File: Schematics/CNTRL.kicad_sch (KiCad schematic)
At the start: 14 parts, among them SW1 RotaryEncoder_Switch, SW2 RotaryEncoder_Switch, SW3 RotaryEncoder_Switch, U5 MCP23017_SP

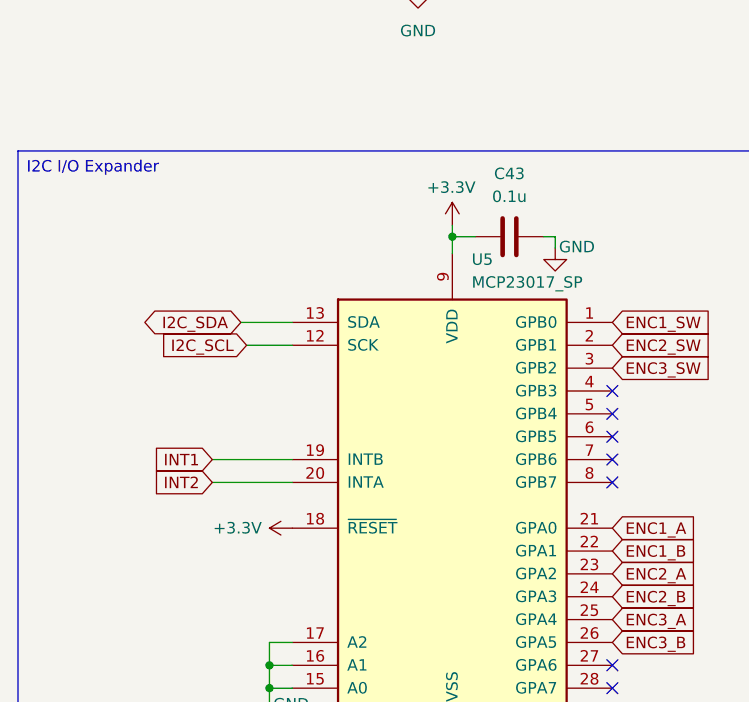
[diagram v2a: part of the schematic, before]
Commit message: Finished PCB routing
New Layout fits perfectly, now all the parts are through-hole and routed together. 20 Vias is a nightmare but better than what we started with
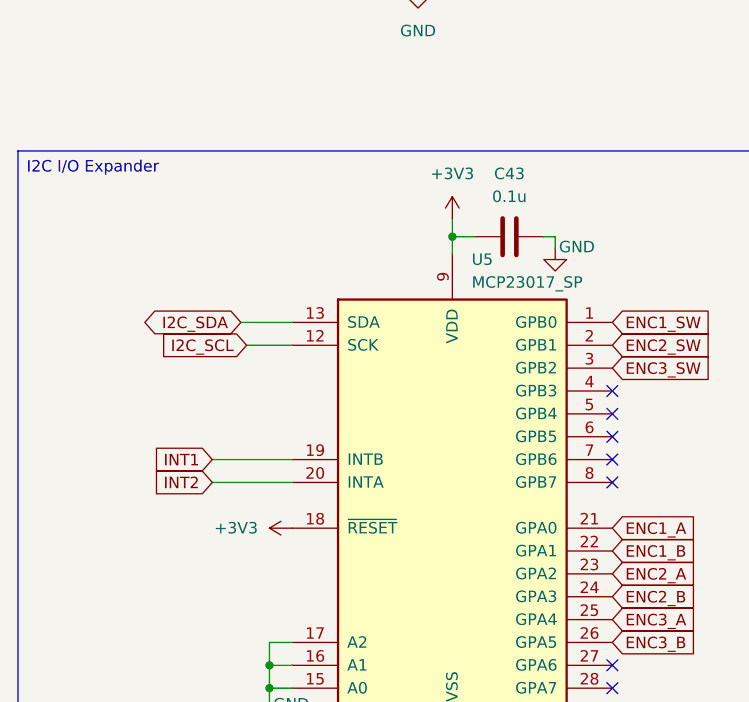
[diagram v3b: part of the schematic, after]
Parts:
- C43: footprint Capacitor_SMD:C_0805_2012Metric_Pad1.18x1.45mm_HandSolder -> Capacitor_THT:C_Disc_D4.7mm_W2.5mm_P5.00mm
- R34, R35, R36, R37, R38, R39, R46, R47, R48: footprint Resistor_SMD:R_0805_2012Metric_Pad1.20x1.40mm_HandSolder -> Resistor_THT:R_Axial_DIN0207_L6.3mm_D2.5mm_P10.16mm_Horizontal
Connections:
- net +3.3V is gone; now on net +3V3: C43.2, U5.18 (~{RESET}), U5.9 (VDD)
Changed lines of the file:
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@@
-	(wire
-		(pts
-			(xy 63.5 130.175) (xy 63.5 131.445)
-		)
-		(stroke
-			(width 0)
-			(type default)
-		)
-	)
 	(wire
 		(pts
@@
 		(pts
 			(xy 151.13 48.895) (xy 190.5 48.895)
+		)
+		(stroke
+			(width 0)
+			(type default)
+		)
+	)
+	(wire
+		(pts
+			(xy 63.5 129.54) (xy 63.5 131.445)
 		)
 		(stroke
@@
 			)
 		)
-		(property "Footprint" "Resistor_SMD:R_0805_2012Metric_Pad1.20x1.40mm_HandSolder"
+		(property "Footprint" "Resistor_THT:R_Axial_DIN0207_L6.3mm_D2.5mm_P10.16mm_Horizontal"
 			(at 46.228 81.915 90)
 			(effects
@@
 			)
 		)
-		(property "Footprint" "Resistor_SMD:R_0805_2012Metric_Pad1.20x1.40mm_HandSolder"
+		(property "Footprint" "Resistor_THT:R_Axial_DIN0207_L6.3mm_D2.5mm_P10.16mm_Horizontal"
 			(at 182.118 40.005 90)
 			(effects
@@
 	)
 	(symbol
-		(lib_id "power:+3.3V")
+		(lib_id "power:+3V3")
+		(at 73.66 36.195 0)
+		(unit 1)
+		(exclude_from_sim no)
+		(in_bom yes)
+		(on_board yes)
+		(dnp no)
+		(fields_autoplaced yes)
+		(property "Reference" "#PWR052"
+			(at 73.66 40.005 0)
+			(effects
+				(font
+					(size 1.27 1.27)
+				)
+				(hide yes)
+			)
+		)
+		(property "Value" "+3V3"
+			(at 73.66 31.115 0)
+			(effects
+				(font
+					(size 1.27 1.27)
+				)
+			)
+		)
+		(property "Footprint" ""
+			(at 73.66 36.195 0)
+			(effects
+				(font
+					(size 1.27 1.27)
+				)
+				(hide yes)
+			)
+		)
+		(property "Datasheet" ""
+			(at 73.66 36.195 0)
+			(effects
+				(font
+					(size 1.27 1.27)
+				)
+				(hide yes)
+			)
+		)
+		(property "Description" "Power symbol creates a global label with name \"+3V3\""
+			(at 73.66 36.195 0)
+			(effects
+				(font
+					(size 1.27 1.27)
+				)
+				(hide yes)
+			)
+		)
+		(pin "1"
+		)
+		(instances
+			(project "Harmoniser HAT"
+				(path "/41751dd2-97f9-4cc6-b9e6-b561e5949053/5d678f4e-03b5-43f5-b100-a64e850a5e5c"
+					(reference "#PWR052")
+					(unit 1)
+				)
+			)
+		)
+	)
+	(symbol
+		(lib_id "power:+3V3")
 		(at 45.72 163.83 90)
 		(unit 1)
@@
 		(on_board yes)
 		(dnp no)
-		(property "Reference" "#PWR0183"
+		(fields_autoplaced yes)
+		(property "Reference" "#PWR018"
 			(at 49.53 163.83 0)
 			(effects
@@
 			)
 		)
-		(property "Value" "+3.3V"
-			(at 39.624 163.83 90)
-			(effects
-				(font
-					(size 1.27 1.27)
-				)
+		(property "Value" "+3V3"
+			(at 41.91 163.8299 90)
+			(effects
+				(font
+					(size 1.27 1.27)
+				)
+				(justify left)
 			)
 		)
@@
 			)
 		)
-		(property "Description" "Power symbol creates a global label with name \"+3.3V\""
+		(property "Description" "Power symbol creates a global label with name \"+3V3\""
 			(at 45.72 163.83 0)
 			(effects
@@
 			(project "Harmoniser HAT"
 				(path "/41751dd2-97f9-4cc6-b9e6-b561e5949053/5d678f4e-03b5-43f5-b100-a64e850a5e5c"
-					(reference "#PWR0183")
-					(unit 1)
-				)
-			)
-		)
-	)
-	(symbol
-		(lib_id "power:+3V3")
-		(at 73.66 36.195 0)
-		(unit 1)
-		(exclude_from_sim no)
-		(in_bom yes)
-		(on_board yes)
-		(dnp no)
-		(fields_autoplaced yes)
-		(property "Reference" "#PWR052"
-			(at 73.66 40.005 0)
-			(effects
-				(font
-					(size 1.27 1.27)
-				)
-				(hide yes)
-			)
-		)
-		(property "Value" "+3V3"
-			(at 73.66 31.115 0)
-			(effects
-				(font
-					(size 1.27 1.27)
-				)
-			)
-		)
-		(property "Footprint" ""
-			(at 73.66 36.195 0)
-			(effects
-				(font
-					(size 1.27 1.27)
-				)
-				(hide yes)
-			)
-		)
-		(property "Datasheet" ""
-			(at 73.66 36.195 0)
-			(effects
-				(font
-					(size 1.27 1.27)
-				)
-				(hide yes)
-			)
-		)
-		(property "Description" "Power symbol creates a global label with name \"+3V3\""
-			(at 73.66 36.195 0)
-			(effects
-				(font
-					(size 1.27 1.27)
-				)
-				(hide yes)
-			)
-		)
-		(pin "1"
-		)
-		(instances
-			(project "Harmoniser HAT"
-				(path "/41751dd2-97f9-4cc6-b9e6-b561e5949053/5d678f4e-03b5-43f5-b100-a64e850a5e5c"
-					(reference "#PWR052")
+					(reference "#PWR018")
 					(unit 1)
 				)
@@
 			)
 		)
-		(property "Footprint" "Resistor_SMD:R_0805_2012Metric_Pad1.20x1.40mm_HandSolder"
+		(property "Footprint" "Resistor_THT:R_Axial_DIN0207_L6.3mm_D2.5mm_P10.16mm_Horizontal"
 			(at 75.438 40.005 90)
 			(effects
@@
 			)
 		)
-		(property "Footprint" "Resistor_SMD:R_0805_2012Metric_Pad1.20x1.40mm_HandSolder"
+		(property "Footprint" "Resistor_THT:R_Axial_DIN0207_L6.3mm_D2.5mm_P10.16mm_Horizontal"
 			(at 46.228 40.005 90)
 			(effects
@@
 			)
 		)
-		(property "Footprint" "Resistor_SMD:R_0805_2012Metric_Pad1.20x1.40mm_HandSolder"
+		(property "Footprint" "Resistor_THT:R_Axial_DIN0207_L6.3mm_D2.5mm_P10.16mm_Horizontal"
 			(at 220.218 40.005 90)
 			(effects
@@
 			)
 		)
-		(property "Footprint" "Capacitor_SMD:C_0805_2012Metric_Pad1.18x1.45mm_HandSolder"
+		(property "Footprint" "Capacitor_THT:C_Disc_D4.7mm_W2.5mm_P5.00mm"
 			(at 66.04 132.4102 0)
 			(effects
@@
 	)
 	(symbol
-		(lib_id "power:+3.3V")
-		(at 63.5 130.175 0)
-		(unit 1)
-		(exclude_from_sim no)
-		(in_bom yes)
-		(on_board yes)
-		(dnp no)
-		(property "Reference" "#PWR0184"
-			(at 63.5 133.985 0)
-			(effects
-				(font
-					(size 1.27 1.27)
-				)
-				(hide yes)
-			)
-		)
-		(property "Value" "+3.3V"
-			(at 63.373 125.984 0)
-			(effects
-				(font
-					(size 1.27 1.27)
-				)
-			)
-		)
-		(property "Footprint" ""
-			(at 63.5 130.175 0)
-			(effects
-				(font
-					(size 1.27 1.27)
-				)
-				(hide yes)
-			)
-		)
-		(property "Datasheet" ""
-			(at 63.5 130.175 0)
-			(effects
-				(font
-					(size 1.27 1.27)
-				)
-				(hide yes)
-			)
-		)
-		(property "Description" "Power symbol creates a global label with name \"+3.3V\""
-			(at 63.5 130.175 0)
-			(effects
-				(font
-					(size 1.27 1.27)
-				)
-				(hide yes)
-			)
-		)
-		(pin "1"
-		)
-		(instances
-			(project "Harmoniser HAT"
-				(path "/41751dd2-97f9-4cc6-b9e6-b561e5949053/5d678f4e-03b5-43f5-b100-a64e850a5e5c"
-					(reference "#PWR0184")
-					(unit 1)
-				)
-			)
-		)
-	)
-	(symbol
 		(lib_id "Device:R")
 		(at 73.66 81.915 180)
@@
 			)
 		)
-		(property "Footprint" "Resistor_SMD:R_0805_2012Metric_Pad1.20x1.40mm_HandSolder"
+		(property "Footprint" "Resistor_THT:R_Axial_DIN0207_L6.3mm_D2.5mm_P10.16mm_Horizontal"
 			(at 75.438 81.915 90)
 			(effects
@@
 			)
 		)
-		(property "Footprint" "Resistor_SMD:R_0805_2012Metric_Pad1.20x1.40mm_HandSolder"
+		(property "Footprint" "Resistor_THT:R_Axial_DIN0207_L6.3mm_D2.5mm_P10.16mm_Horizontal"
 			(at 152.908 40.005 90)
 			(effects
@@
 			)
 		)
-		(property "Footprint" "Resistor_SMD:R_0805_2012Metric_Pad1.20x1.40mm_HandSolder"
+		(property "Footprint" "Resistor_THT:R_Axial_DIN0207_L6.3mm_D2.5mm_P10.16mm_Horizontal"
 			(at 113.538 40.005 90)
 			(effects
@@
 	)
 	(symbol
+		(lib_id "power:+3V3")
+		(at 63.5 129.54 0)
+		(unit 1)
+		(exclude_from_sim no)
+		(in_bom yes)
+		(on_board yes)
+		(dnp no)
+		(fields_autoplaced yes)
+		(property "Reference" "#PWR019"
+			(at 63.5 133.35 0)
+			(effects
+				(font
+					(size 1.27 1.27)
+				)
+				(hide yes)
+			)
+		)
+		(property "Value" "+3V3"
+			(at 63.5 124.46 0)
+			(effects
+				(font
+					(size 1.27 1.27)
+				)
+			)
+		)
+		(property "Footprint" ""
+			(at 63.5 129.54 0)
+			(effects
+				(font
+					(size 1.27 1.27)
+				)
+				(hide yes)
+			)
+		)
+		(property "Datasheet" ""
+			(at 63.5 129.54 0)
+			(effects
+				(font
+					(size 1.27 1.27)
+				)
+				(hide yes)
+			)
+		)
+		(property "Description" "Power symbol creates a global label with name \"+3V3\""
+			(at 63.5 129.54 0)
+			(effects
+				(font
+					(size 1.27 1.27)
+				)
+				(hide yes)
+			)
+		)
+		(pin "1"
+		)
+		(instances
+			(project "Harmoniser HAT"
+				(path "/41751dd2-97f9-4cc6-b9e6-b561e5949053/5d678f4e-03b5-43f5-b100-a64e850a5e5c"
+					(reference "#PWR019")
+					(unit 1)
+				)
+			)
+		)
+	)
+	(symbol
 		(lib_id "power:GND")
 		(at 99.06 61.595 0)
@@
 			)
 		)
-		(property "Footprint" "Resistor_SMD:R_0805_2012Metric_Pad1.20x1.40mm_HandSolder"
+		(property "Footprint" "Resistor_THT:R_Axial_DIN0207_L6.3mm_D2.5mm_P10.16mm_Horizontal"
 			(at 113.538 81.915 90)
 			(effects

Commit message: Tidied up Schematic
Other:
- moved on the sheet: C43, R46, R47, R48, SW3, U5
